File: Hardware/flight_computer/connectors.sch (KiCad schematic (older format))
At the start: 8 parts

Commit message: added more components
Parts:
- removed J?: Conn_02x03_Counter_Clockwise, symbol Connector_Generic:Conn_02x03_Counter_Clockwise
- added J?: Conn_02x03, drone_footprints:TSW-103-07-F-D, symbol openDrone_parts:Conn_02x03
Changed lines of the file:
@@
 Text Notes 850  1650 0    50   ~ 0
 ESC Connection
-$Comp
-L Connector_Generic:Conn_02x03_Counter_Clockwise J?
-U 1 1 5F76BFE5
-P 3850 1250
-F 0 "J?" H 4150 1550 50  0000 C CNN
-F 1 "Conn_02x03_Counter_Clockwise" H 4300 1500 50  0001 C CNN
-F 2 "" H 3850 1250 50  0001 C CNN
-F 3 "~" H 3850 1250 50  0001 C CNN
-	1    3850 1250
-	1    0    0    -1
-$EndComp
 Text Notes 3700 1550 0    50   ~ 0
 Debug Port
@@
 Text GLabel 4150 1350 2    50   Input ~ 0
 SWDIO
+$Comp
+L openDrone_parts:Conn_02x03 J?
+U 1 1 5F7B4CC5
+P 3850 1250
+F 0 "J?" H 3900 1567 50  0000 C CNN
+F 1 "Conn_02x03" H 3900 1476 50  0000 C CNN
+F 2 "drone_footprints:TSW-103-07-F-D" H 4650 1450 50  0001 C CNN
+F 3 "~" H 3850 1250 50  0001 C CNN
+	1    3850 1250
+	1    0    0    -1
+$EndComp
 $EndSCHEMATC

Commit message: Updates stm to connectors
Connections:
- net labels added: FMU_USART8_RX, FMU_USART8_TX, rx_frsky, tx_frsky
- net labels removed: VCC, rx_frysky, tx_frysky
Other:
- note added: "FrSky Telemetry/Serial 4\n"
- note removed: "FrySky Telemetry/Serial 4\n"
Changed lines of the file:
@@
 $Descr A4 11693 8268
 encoding utf-8
-Sheet 10 10
+Sheet 6 6
 Title ""
 Date ""
@@
 Text Notes 1000 2950 0    50   ~ 0
 TELEM1
-$Comp
-L power:VCC #PWR?
-U 1 1 5F77B61C
-P 1550 2000
-F 0 "#PWR?" H 1550 1850 50  0001 C CNN
-F 1 "VCC" H 1567 2173 50  0000 C CNN
-F 2 "" H 1550 2000 50  0001 C CNN
-F 3 "" H 1550 2000 50  0001 C CNN
-	1    1550 2000
-	1    0    0    -1
-$EndComp
 Text HLabel 1400 2400 2    50   Input ~ 0
 tx_telem_1
@@
 $EndComp
 Text Notes 650  4250 0    50   ~ 0
-FrySky Telemetry/Serial 4\n
+FrSky Telemetry/Serial 4\n
 Wire Wire Line
 	1400 4100 1750 4100
@@
 	1    0    0    -1
 $EndComp
-Text HLabel 1400 3900 2    50   Input ~ 0
-tx_frysky
-Text HLabel 1400 4000 2    50   Input ~ 0
-rx_frysky
 $Comp
 L openDrone_parts:JST_GH_5_RA J?
@@
 	1    0    0    -1
 $EndComp
-$Comp
-L power:VCC #PWR?
-U 1 1 5F77F49C
-P 1650 4950
-F 0 "#PWR?" H 1650 4800 50  0001 C CNN
-F 1 "VCC" H 1667 5123 50  0000 C CNN
-F 2 "" H 1650 4950 50  0001 C CNN
-F 3 "" H 1650 4950 50  0001 C CNN
-	1    1650 4950
-	1    0    0    -1
-$EndComp
 Text HLabel 1450 5150 2    50   Input ~ 0
 rc_in
 Text HLabel 2000 5250 2    50   Input ~ 0
 rssi_in
-Text GLabel 1450 5350 2    50   Input ~ 0
-3V3
 Wire Wire Line
 	1400 2300 1550 2300
@@
 	-1   0    0    1
 $EndComp
-$Comp
-L power:VCC #PWR?
-U 1 1 5F785954
-P 1550 3500
-F 0 "#PWR?" H 1550 3350 50  0001 C CNN
-F 1 "VCC" H 1700 3550 50  0000 C CNN
-F 2 "" H 1550 3500 50  0001 C CNN
-F 3 "" H 1550 3500 50  0001 C CNN
-	1    1550 3500
-	1    0    0    -1
-$EndComp
 Wire Wire Line
 	1400 3800 1550 3800
@@
 Wire Wire Line
 	1450 5250 1700 5250
-Text GLabel 3650 1250 0    50   Input ~ 0
-FMU_UART7_TX
-Text GLabel 3650 1350 0    50   Input ~ 0
-FMU_UART7_RX
-Text GLabel 3650 1150 0    50   Input ~ 0
-3V3
-Text GLabel 4150 1250 2    50   Input ~ 0
-SWCLK
-Text GLabel 4150 1350 2    50   Input ~ 0
-SWDIO
 $Comp
 L openDrone_parts:Conn_02x03 J?
@@
 	1    0    0    -1
 $EndComp
+Text HLabel 3650 1350 0    50   Input ~ 0
+FMU_UART7_RX
+Text HLabel 3650 1250 0    50   Input ~ 0
+FMU_UART7_TX
+Text HLabel 4150 1250 2    50   Input ~ 0
+SWCLK
+Text HLabel 4150 1350 2    50   Input ~ 0
+SWDIO
+Text HLabel 3650 1150 0    50   Input ~ 0
+3V3
+Text HLabel 1450 5350 2    50   Input ~ 0
+3V3
+Text Label 1400 3900 0    50   ~ 0
+tx_frsky
+Text Label 1400 4000 0    50   ~ 0
+rx_frsky
+Text HLabel 3650 3750 0    50   Input ~ 0
+FMU_USART8_TX
+Text HLabel 3650 3850 0    50   Input ~ 0
+FMU_USART8_RX
+$Comp
+L power:GND #PWR?
+U 1 1 5F8EE166
+P 1650 4950
+F 0 "#PWR?" H 1650 4700 50  0001 C CNN
+F 1 "GND" H 1655 4777 50  0000 C CNN
+F 2 "" H 1650 4950 50  0001 C CNN
+F 3 "" H 1650 4950 50  0001 C CNN
+	1    1650 4950
+	-1   0    0    1
+$EndComp
+$Comp
+L power:GND #PWR?
+U 1 1 5F8EE646
+P 1550 3500
+F 0 "#PWR?" H 1550 3250 50  0001 C CNN
+F 1 "GND" H 1555 3327 50  0000 C CNN
+F 2 "" H 1550 3500 50  0001 C CNN
+F 3 "" H 1550 3500 50  0001 C CNN
+	1    1550 3500
+	-1   0    0    1
+$EndComp
+$Comp
+L power:GND #PWR?
+U 1 1 5F8EE993
+P 1550 2000
+F 0 "#PWR?" H 1550 1750 50  0001 C CNN
+F 1 "GND" H 1555 1827 50  0000 C CNN
+F 2 "" H 1550 2000 50  0001 C CNN
+F 3 "" H 1550 2000 50  0001 C CNN
+	1    1550 2000
+	-1   0    0    1
+$EndComp
 $EndSCHEMATC

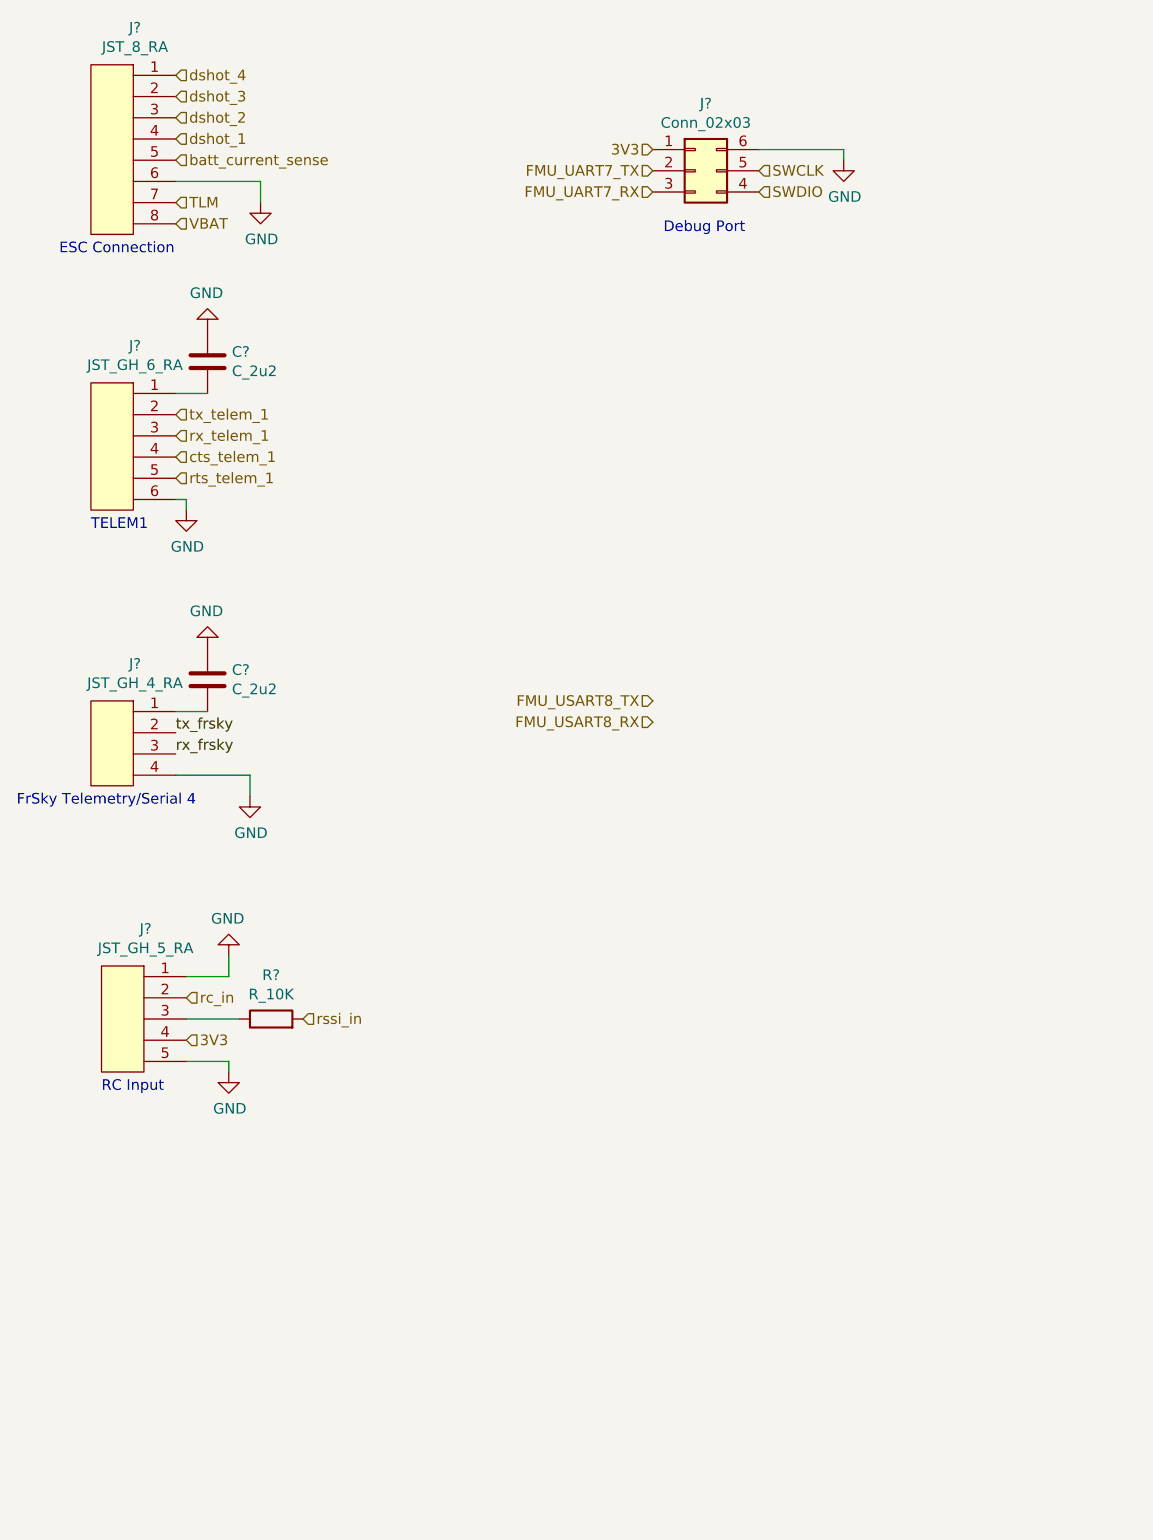
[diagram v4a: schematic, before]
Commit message: Updates drdy pins and rc connections
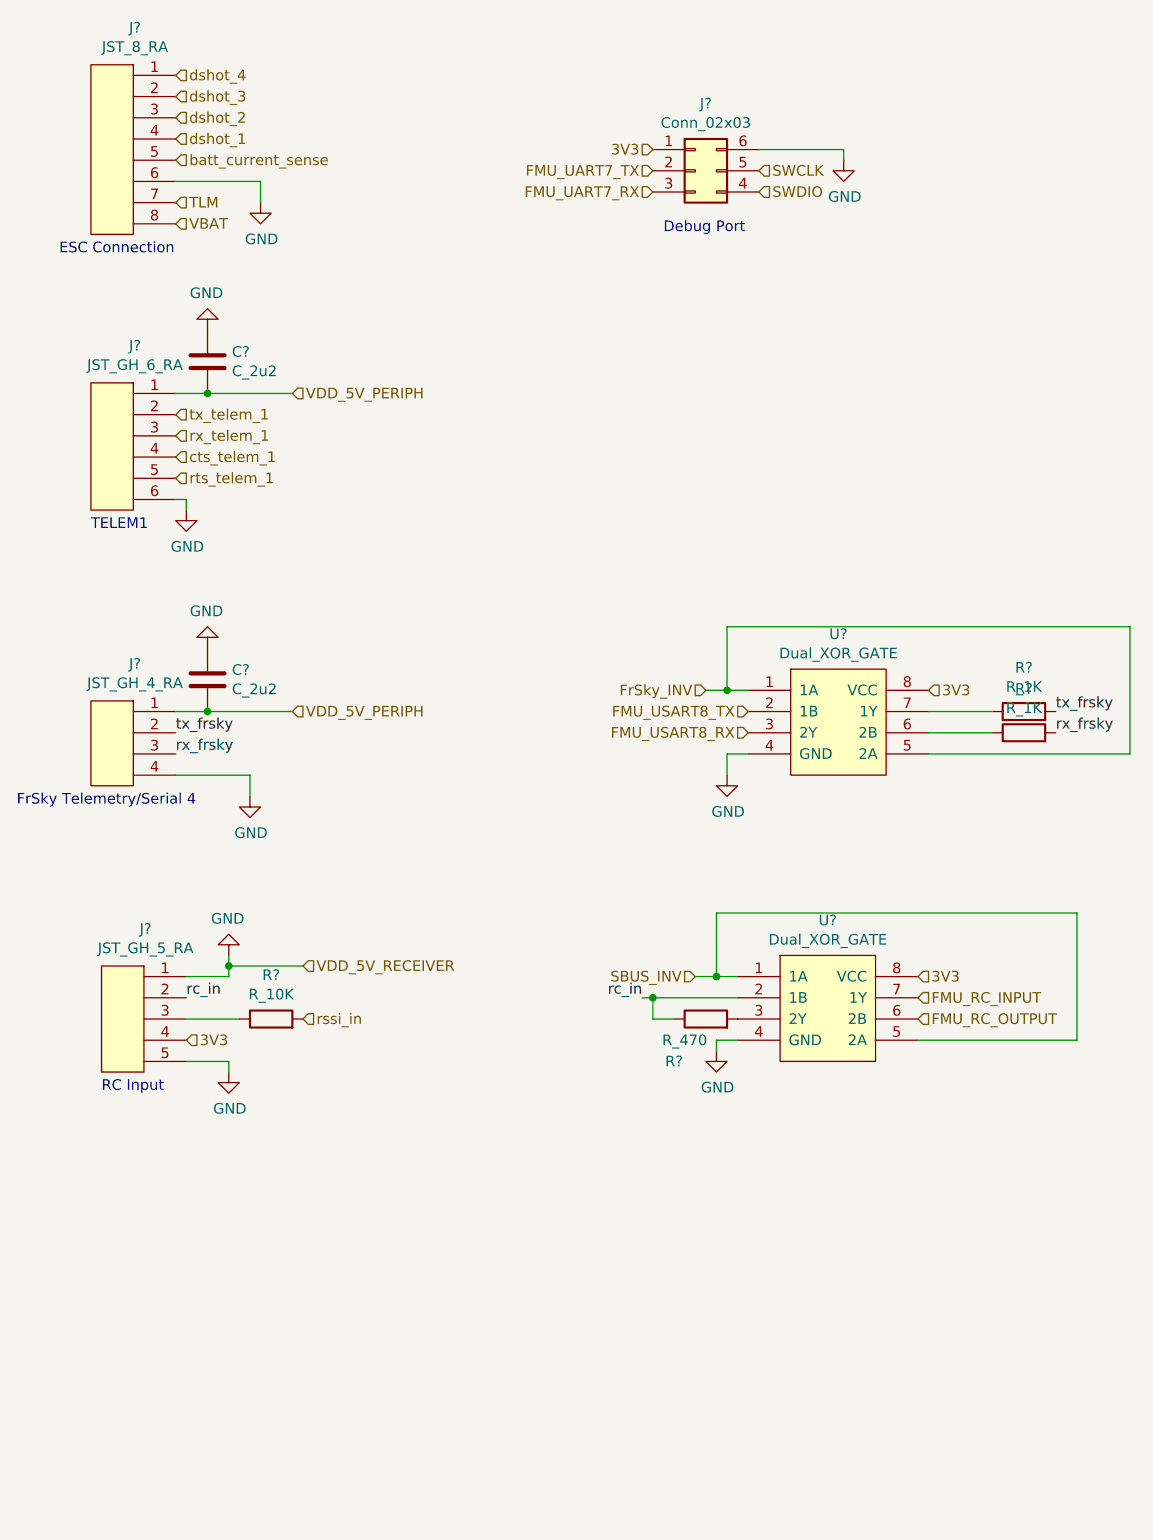
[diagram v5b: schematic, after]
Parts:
- added R? (x2): R_1K, Resistors_SMD:R_0805, symbol openDrone_parts:R_1K
- added R?: R_470, Resistors_SMD:R_0805, symbol openDrone_parts:R_470
- added U? (x2): Dual_XOR_GATE, Housings_SSOP:TSSOP-8_3x3mm_Pitch0.65mm, symbol openDrone_parts:Dual_XOR_GATE
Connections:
- net 3V3: now also U?.8 (VCC), U?.8 (VCC)
- net FMU_USART8_RX: now also U?.3 (2Y)
- net FMU_USART8_TX: now also U?.2 (1B)
- net GND: now also U?.4 (GND), U?.4 (GND)
- net rc_in: now also R?.1, U?.2 (1B)
- net rx_frsky: now also R?.2
- net tx_frsky: now also R?.2
- net VDD_5V_PERIPH: now reaches C?.1, J?.1
- net VDD_5V_PERIPH: now also C?.1, J?.1
- new net: R?.1, U?.6 (2B)
- new net: R?.1, U?.7 (1Y)
- new net: R?.2, U?.3 (2Y)
- new net FMU_RC_INPUT: U?.7 (1Y)
- new net FMU_RC_OUTPUT: U?.6 (2B)
- new net FrSky_INV: U?.1 (1A), U?.5 (2A)
- new net SBUS_INV: U?.1 (1A), U?.5 (2A)
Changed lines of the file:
@@
 	1450 5050 1650 5050
 Wire Wire Line
-	1650 5050 1650 4950
+	1650 5050 1650 5000
 Wire Wire Line
 	1450 5450 1650 5450
@@
 	1    0    0    -1
 $EndComp
-Text HLabel 1450 5150 2    50   Input ~ 0
-rc_in
 Text HLabel 2000 5250 2    50   Input ~ 0
 rssi_in
@@
 Text Label 1400 4000 0    50   ~ 0
 rx_frsky
-Text HLabel 3650 3750 0    50   Input ~ 0
+Text HLabel 4100 3800 0    50   Input ~ 0
 FMU_USART8_TX
-Text HLabel 3650 3850 0    50   Input ~ 0
+Text HLabel 4100 3900 0    50   Input ~ 0
 FMU_USART8_RX
 $Comp
@@
 	-1   0    0    1
 $EndComp
+$Comp
+L openDrone_parts:Dual_XOR_GATE U?
+U 1 1 5F7FAE6E
+P 4300 3700
+F 0 "U?" H 4525 3965 50  0000 C CNN
+F 1 "Dual_XOR_GATE" H 4525 3874 50  0000 C CNN
+F 2 "Housings_SSOP:TSSOP-8_3x3mm_Pitch0.65mm" H 5100 4150 50  0001 C CNN
+F 3 "" H 4300 3700 50  0001 C CNN
+F 4 "1727-5995-1-ND" H 4550 4050 50  0001 C CNN "DPN"
+F 5 "74LVC2G86DP,125" H 4500 3950 50  0001 C CNN "MPN"
+	1    4300 3700
+	1    0    0    -1
+$EndComp
+$Comp
+L openDrone_parts:R_1K R?
+U 1 1 5F7FC1DD
+P 5400 3800
+F 0 "R?" H 5400 4007 50  0000 C CNN
+F 1 "R_1K" H 5400 3916 50  0000 C CNN
+F 2 "Resistors_SMD:R_0805" H 4600 3950 50  0001 C CNN
+F 3 "" H 5100 4300 50  0001 C CNN
+F 4 "311-1.0KARCT-ND" H 4750 4050 60  0001 C CNN "DPN"
+	1    5400 3800
+	1    0    0    -1
+$EndComp
+$Comp
+L openDrone_parts:R_1K R?
+U 1 1 5F7FCD82
+P 5400 3900
+F 0 "R?" H 5400 4107 50  0000 C CNN
+F 1 "R_1K" H 5400 4016 50  0000 C CNN
+F 2 "Resistors_SMD:R_0805" H 4600 4050 50  0001 C CNN
+F 3 "" H 5100 4400 50  0001 C CNN
+F 4 "311-1.0KARCT-ND" H 4750 4150 60  0001 C CNN "DPN"
+	1    5400 3900
+	1    0    0    -1
+$EndComp
+Wire Wire Line
+	5250 3800 4950 3800
+Wire Wire Line
+	4950 3900 5250 3900
+Text Label 5550 3900 0    50   ~ 0
+rx_frsky
+Text Label 5550 3800 0    50   ~ 0
+tx_frsky
+$Comp
+L power:GND #PWR?
+U 1 1 5F7FD63E
+P 4000 4100
+F 0 "#PWR?" H 4000 3850 50  0001 C CNN
+F 1 "GND" H 4005 3927 50  0000 C CNN
+F 2 "" H 4000 4100 50  0001 C CNN
+F 3 "" H 4000 4100 50  0001 C CNN
+	1    4000 4100
+	1    0    0    -1
+$EndComp
+Wire Wire Line
+	4100 4000 4000 4000
+Wire Wire Line
+	4000 4000 4000 4100
+Text HLabel 4950 3700 2    50   Input ~ 0
+3V3
+Text HLabel 3900 3700 0    50   Input ~ 0
+FrSky_INV
+Wire Wire Line
+	3900 3700 4000 3700
+Wire Wire Line
+	4000 3700 4000 3400
+Wire Wire Line
+	4000 3400 5900 3400
+Wire Wire Line
+	5900 3400 5900 4000
+Wire Wire Line
+	5900 4000 4950 4000
+Connection ~ 4000 3700
+Wire Wire Line
+	4000 3700 4100 3700
+$Comp
+L openDrone_parts:Dual_XOR_GATE U?
+U 1 1 5F7FEBF9
+P 4250 5050
+F 0 "U?" H 4475 5315 50  0000 C CNN
+F 1 "Dual_XOR_GATE" H 4475 5224 50  0000 C CNN
+F 2 "Housings_SSOP:TSSOP-8_3x3mm_Pitch0.65mm" H 5050 5500 50  0001 C CNN
+F 3 "" H 4250 5050 50  0001 C CNN
+F 4 "1727-5995-1-ND" H 4500 5400 50  0001 C CNN "DPN"
+F 5 "74LVC2G86DP,125" H 4450 5300 50  0001 C CNN "MPN"
+	1    4250 5050
+	1    0    0    -1
+$EndComp
+Text HLabel 1950 3800 2    50   Input ~ 0
+VDD_5V_PERIPH
+Wire Wire Line
+	1950 3800 1550 3800
+Connection ~ 1550 3800
+Text HLabel 1950 2300 2    50   Input ~ 0
+VDD_5V_PERIPH
+Wire Wire Line
+	1950 2300 1550 2300
+Connection ~ 1550 2300
+Text HLabel 2000 5000 2    50   Input ~ 0
+VDD_5V_RECEIVER
+Wire Wire Line
+	2000 5000 1650 5000
+Connection ~ 1650 5000
+Wire Wire Line
+	1650 5000 1650 4950
+$Comp
+L power:GND #PWR?
+U 1 1 5F801583
+P 3950 5400
+F 0 "#PWR?" H 3950 5150 50  0001 C CNN
+F 1 "GND" H 3955 5227 50  0000 C CNN
+F 2 "" H 3950 5400 50  0001 C CNN
+F 3 "" H 3950 5400 50  0001 C CNN
+	1    3950 5400
+	1    0    0    -1
+$EndComp
+Wire Wire Line
+	4050 5350 3950 5350
+Wire Wire Line
+	3950 5350 3950 5400
+Text HLabel 4900 5050 2    50   Input ~ 0
+3V3
+Text HLabel 4900 5250 2    50   Input ~ 0
+FMU_RC_OUTPUT
+Text HLabel 4900 5150 2    50   Input ~ 0
+FMU_RC_INPUT
+Text HLabel 3850 5050 0    50   Input ~ 0
+SBUS_INV
+Wire Wire Line
+	3850 5050 3950 5050
+Wire Wire Line
+	3950 5050 3950 4750
+Wire Wire Line
+	3950 4750 5650 4750
+Wire Wire Line
+	5650 4750 5650 5350
+Wire Wire Line
+	5650 5350 4900 5350
+Connection ~ 3950 5050
+Wire Wire Line
+	3950 5050 4050 5050
+$Comp
+L openDrone_parts:R_470 R?
+U 1 1 5F8039A4
+P 3900 5250
+F 0 "R?" H 3750 5050 50  0000 C CNN
+F 1 "R_470" H 3800 5150 50  0000 C CNN
+F 2 "Resistors_SMD:R_0805" H 3100 5400 50  0001 C CNN
+F 3 "" H 3600 5750 50  0001 C CNN
+F 4 "A129745CT-ND" H 3250 5500 60  0001 C CNN "DPN"
+	1    3900 5250
+	1    0    0    -1
+$EndComp
+Wire Wire Line
+	3600 5150 3650 5150
+Wire Wire Line
+	3750 5250 3650 5250
+Wire Wire Line
+	3650 5250 3650 5150
+Connection ~ 3650 5150
+Wire Wire Line
+	3650 5150 4050 5150
+Text Label 1450 5150 0    50   ~ 0
+rc_in
+Text Label 3600 5150 2    50   ~ 0
+rc_in
 $EndSCHEMATC

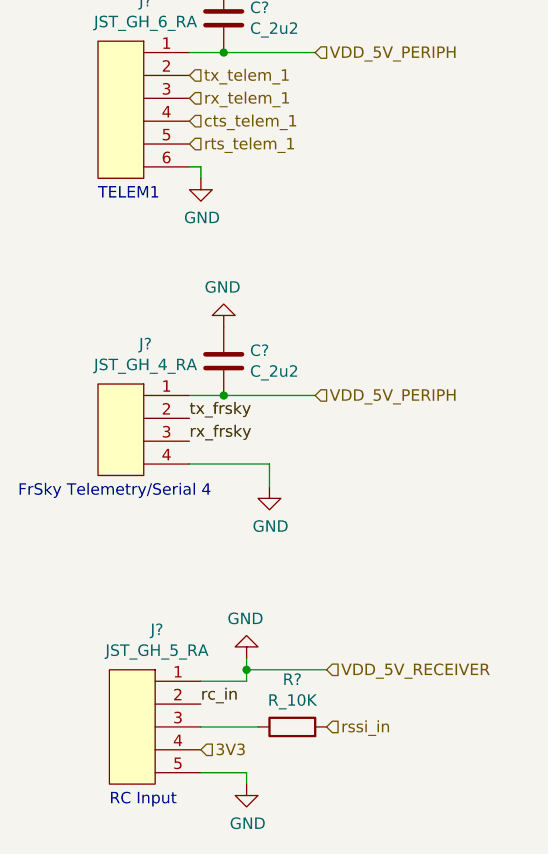
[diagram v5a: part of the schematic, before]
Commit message: Adds buck converters
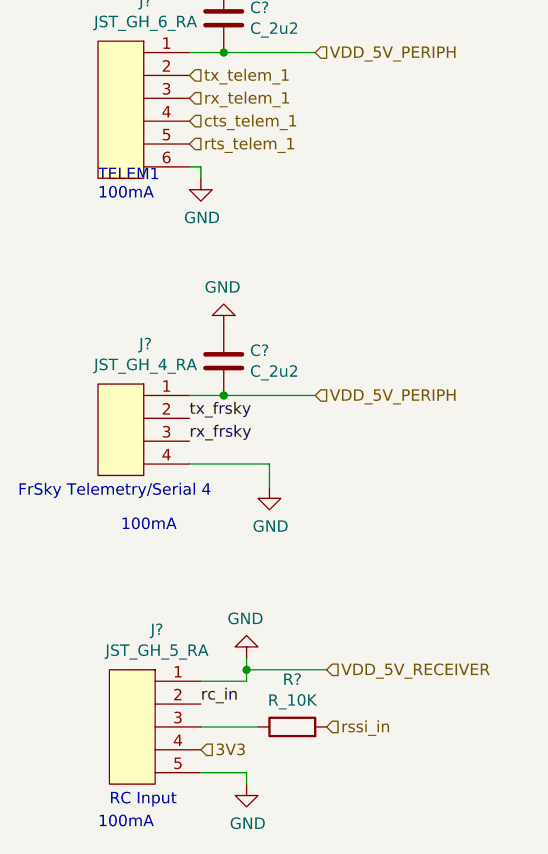
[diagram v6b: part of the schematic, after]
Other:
- note added: "100mA"
- note added: "TELEM1\n100mA"
- note removed: "TELEM1"
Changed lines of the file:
@@
 $EndComp
 Text Notes 1000 2950 0    50   ~ 0
-TELEM1
+TELEM1\n100mA
 Text HLabel 1400 2400 2    50   Input ~ 0
 tx_telem_1
@@
 Text Label 3600 5150 2    50   ~ 0
 rc_in
+Text Notes 1100 4400 0    50   ~ 0
+100mA
+Text Notes 1000 5700 0    50   ~ 0
+100mA
 $EndSCHEMATC

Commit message: added components, rerranged things to slow down dan
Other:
- note added: "BATTERY = VBAT\nBUCK CONVERTER OUTPUT (VDD_5V_BRICK) = VDD_5V_BUCK\nUSB POWER (VBUS) = VDD_5V_USB\nRADIO 5V (VDD_5V_RECEIVER) = VDD_5V_RADIO\nGENERAL 5V (VDD_5V_IN) = VDD_5V_IN\nTELEM/FRSKY (VDD_5V_PERIPH) = VDD_5V_TELEM\nSTM POWER (FMU_VDD_3V3) = VDD_3V3_STM\nSENSORS POWER (VDD_3V3_SENSORS) = VDD_3V3_SENSORS\nRADIO POWER (VDD_3V3_SPEKTRUM) = RADIO_VDD_3V3\n"
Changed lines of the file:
@@
 $Descr A4 11693 8268
 encoding utf-8
-Sheet 4 4
+Sheet 4 5
 Title ""
 Date ""
@@
 Text Notes 1000 5700 0    50   ~ 0
 100mA
+Text Notes 850  7600 0    79   ~ 0
+BATTERY = VBAT\nBUCK CONVERTER OUTPUT (VDD_5V_BRICK) = VDD_5V_BUCK\nUSB POWER (VBUS) = VDD_5V_USB\nRADIO 5V (VDD_5V_RECEIVER) = VDD_5V_RADIO\nGENERAL 5V (VDD_5V_IN) = VDD_5V_IN\nTELEM/FRSKY (VDD_5V_PERIPH) = VDD_5V_TELEM\nSTM POWER (FMU_VDD_3V3) =  VDD_3V3_STM\nSENSORS POWER (VDD_3V3_SENSORS) = VDD_3V3_SENSORS\nRADIO POWER  (VDD_3V3_SPEKTRUM) = RADIO_VDD_3V3\n
 $EndSCHEMATC
